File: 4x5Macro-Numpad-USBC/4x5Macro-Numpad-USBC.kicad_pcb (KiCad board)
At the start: 2 copper layers, 41 parts, among them J1 USB-C, SW1 PROG, SW10 [3,2], SW11 [3,3], SW12 [2,0], SW13 [2,1], SW14 [2,2], SW15 [2,3], SW16 [1,3], SW17 [1,0]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

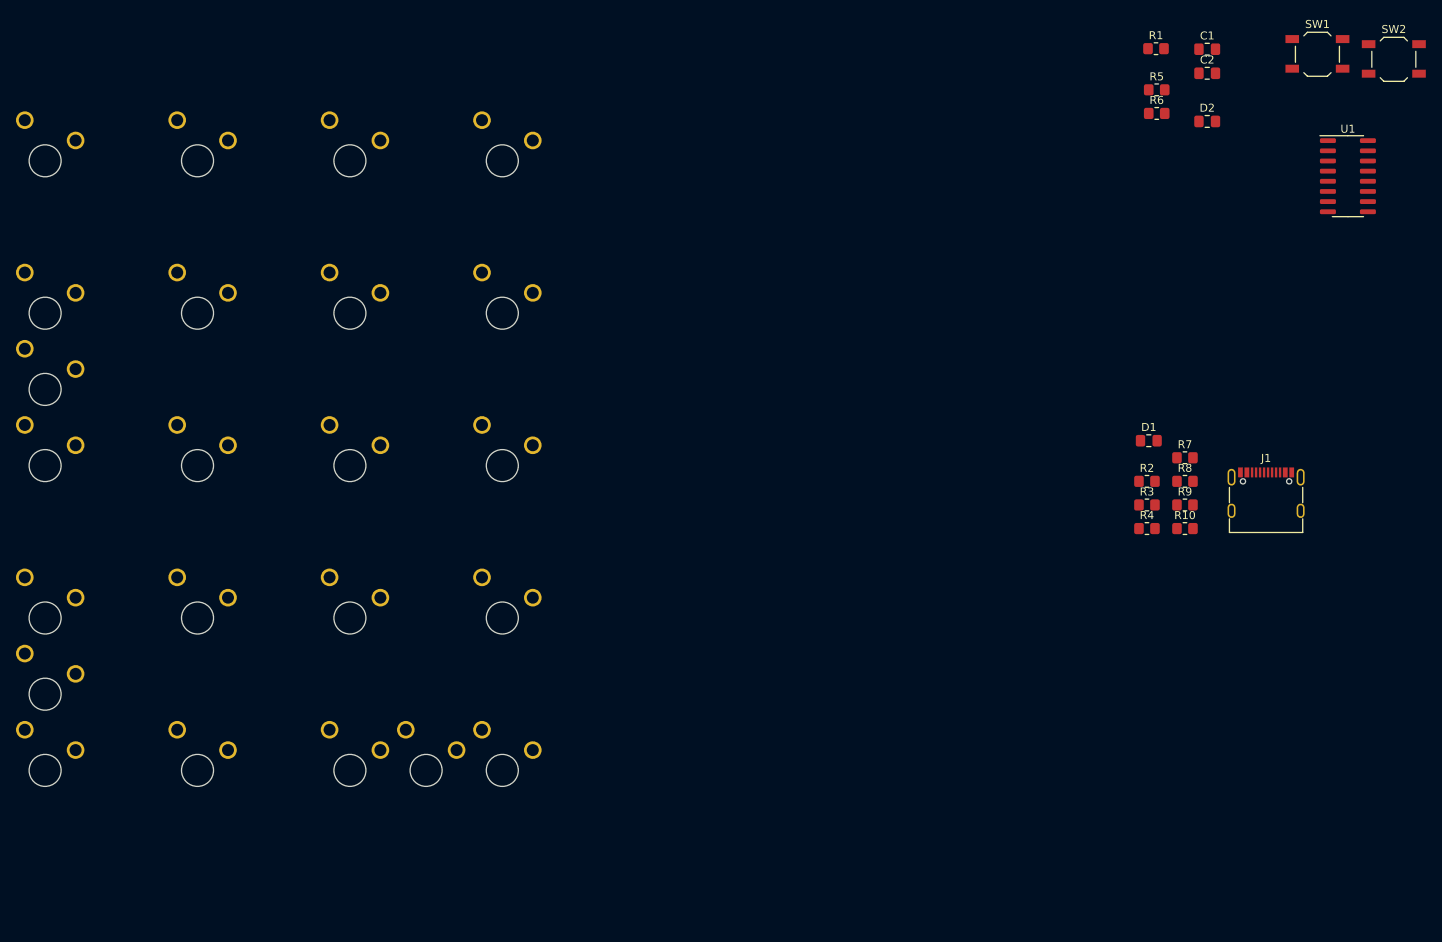
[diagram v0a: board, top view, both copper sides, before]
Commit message: fin+check sch, route pcb, silkscreen todo
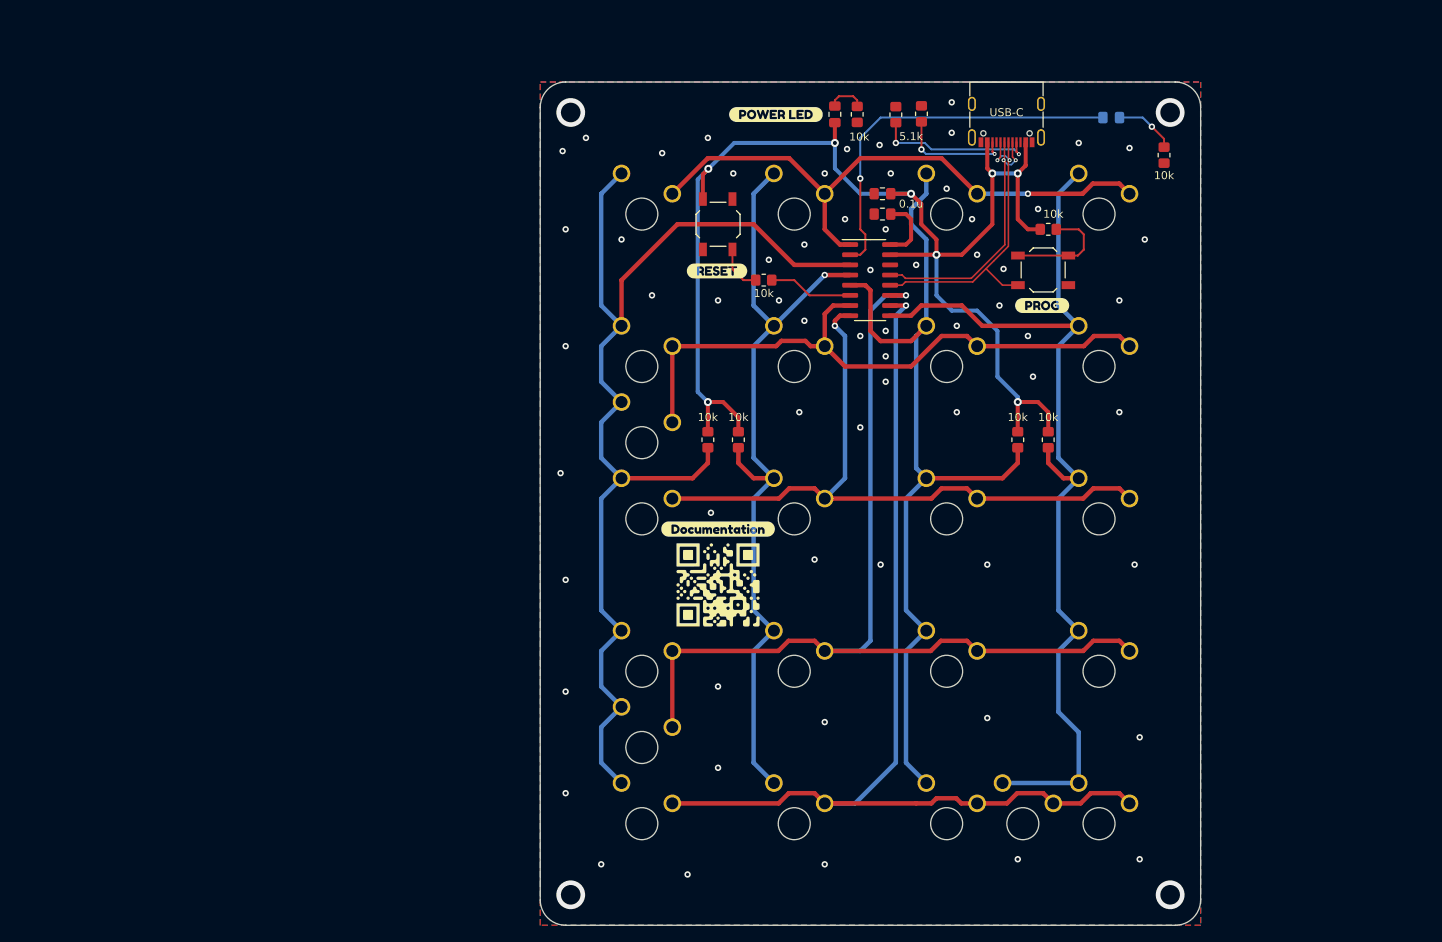
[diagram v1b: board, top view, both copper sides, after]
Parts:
- added G***: LOGO, custom:4x5Macro-Numpad-USBC-qrcode-15x15mm, F.Cu at (132.7, 94.6)
- added kibuzzard-64E3BE21: G***, kibuzzard-64E3BE21, B.Cu at (181.9, 34.0)
- added kibuzzard-64E3BEC4: G***, kibuzzard-64E3BEC4, B.Cu at (139.1, 35.6)
- added kibuzzard-64E42557: G***, kibuzzard-64E42557, F.Cu at (140.0, 35.8)
- added kibuzzard-64E425AB: G***, kibuzzard-64E425AB, F.Cu at (173.2, 59.7)
- added kibuzzard-64E425E5: G***, kibuzzard-64E425E5, F.Cu at (132.6, 55.4)
- added kibuzzard-64E429DF: G***, kibuzzard-64E429DF, F.Cu at (132.7, 87.6)
- D2: moved to B.Cu
- moved SW2 87.0 mm to (132.7, 49.5), turned to 90 degrees
- moved SW12 74.9 mm to (177.8, 81.3)
- moved SW17 74.9 mm to (177.8, 100.3)
- moved SW20 74.9 mm to (120.7, 109.9)
- moved SW25 74.9 mm to (177.8, 119.4)
- moved SW3 74.9 mm to (177.8, 43.2)
- moved SW8 74.9 mm to (177.8, 62.2)
- moved SW11 74.9 mm to (120.7, 62.2)
- moved SW13 74.9 mm to (158.8, 81.3)
- moved SW15 74.9 mm to (120.7, 81.3)
- moved SW16 74.9 mm to (120.7, 100.3)
- moved SW18 74.9 mm to (158.8, 100.3)
- moved SW21 74.9 mm to (168.3, 119.4)
- moved SW22 74.9 mm to (158.8, 119.4)
- moved SW24 74.9 mm to (120.7, 119.4)
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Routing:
- net VBUS: track 0.00 -> 166.0 mm, vias 0 -> 8
- net COL3: track 0.00 -> 141.6 mm
- net ROW0: track 0.00 -> 131.5 mm, vias 0 -> 1
- net COL0: track 0.00 -> 125.8 mm
- net ROW1: track 0.00 -> 124.6 mm, vias 0 -> 1
- net COL1: track 0.00 -> 113.3 mm
- net COL2: track 0.00 -> 103.9 mm, vias 0 -> 1
- net ROW2: track 0.00 -> 86.3 mm, vias 0 -> 1
- net ROW3: track 0.00 -> 79.1 mm
- net ROW4: track 0.00 -> 74.0 mm, vias 0 -> 1
- net /USR_LED: track 0.00 -> 47.8 mm, vias 0 -> 1
- net D+: track 0.00 -> 39.2 mm, vias 0 -> 2
- net D-: track 0.00 -> 33.6 mm, vias 0 -> 2
- net Net-(J1-CC1): track 0.00 -> 20.1 mm, vias 0 -> 2
- net Net-(J1-CC2): track 0.00 -> 14.4 mm, vias 0 -> 2
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- added copper zone on B.Cu, net GND
- added copper zone on F.Cu, net GND
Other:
- board outline added: 82.5 x 105.4 mm

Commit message: mask done, first board revision
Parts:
- removed kibuzzard-64E429DF: G***, kibuzzard-64E429DF
- added COL0: TestPoint_Pad_D2.0mm, TestPoint:TestPoint_Pad_D2.0mm, F.Cu at (174.0, 81.3)
- added COL1: TestPoint_Pad_D2.0mm, TestPoint:TestPoint_Pad_D2.0mm, F.Cu at (170.2, 81.3)
- added COL2: TestPoint_Pad_D2.0mm, TestPoint:TestPoint_Pad_D2.0mm, F.Cu at (135.3, 81.3)
- added COL3: TestPoint_Pad_D2.0mm, TestPoint:TestPoint_Pad_D2.0mm, F.Cu at (131.4, 81.3)
- added GND: TestPoint_Pad_D2.0mm, TestPoint:TestPoint_Pad_D2.0mm, F.Cu at (130.8, 69.2)
- added ROW0: TestPoint_Pad_D2.0mm, TestPoint:TestPoint_Pad_D2.0mm, F.Cu at (151.8, 121.9)
- added ROW1: TestPoint_Pad_D2.0mm, TestPoint:TestPoint_Pad_D2.0mm, F.Cu at (151.8, 102.9)
- added ROW2: TestPoint_Pad_D2.0mm, TestPoint:TestPoint_Pad_D2.0mm, F.Cu at (151.8, 83.8)
- added ROW3: TestPoint_Pad_D2.0mm, TestPoint:TestPoint_Pad_D2.0mm, F.Cu at (151.8, 67.3)
- added ROW4: TestPoint_Pad_D2.0mm, TestPoint:TestPoint_Pad_D2.0mm, F.Cu at (153.0, 41.3)
- added VBUS: TestPoint_Pad_D2.0mm, TestPoint:TestPoint_Pad_D2.0mm, F.Cu at (135.3, 71.8)
- added kibuzzard-64E562F3: G***, kibuzzard-64E562F3, F.Cu at (131.4, 87.0)
- moved G*** 1.27 mm to (131.4, 94.6)
- moved C1 0.64 mm to (153.3, 48.9)
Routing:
- net VBUS: track 166.0 -> 167.1 mm
- net COL3: track 141.6 -> 142.7 mm
- net COL2: track 103.9 -> 105.0 mm
- net COL1: track 113.3 -> 114.5 mm
- net COL0: track 125.8 -> 126.9 mm
- net Net-(U1-CAP): track 8.23 -> 7.59 mm
- net /USR_LED: track 47.8 -> 48.3 mm
- net GND: vias 64 -> 68
- net (no net): vias 4 -> 0
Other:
- board text added: "4x5Macro-Numpad-USBC by edwwardk based on tobychui's design"
- board text added: "JLCJLCJLCJLC"
- board text added: "P11"
- board text added: "P15"
- board text added: "P16"
- board text added: "P17"
- board text added: "P30"
- board text added: "P31"
- board text added: "P32"
- board text added: "P33"
- board text added: "P34"
- board text added: "USR_LED: P14"
- board text added: "rows are active low columns input pulled high by default"
- board text added: "v1.0"
